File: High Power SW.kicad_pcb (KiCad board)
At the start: 2 copper layers, 48 x 48 mm, 19 parts

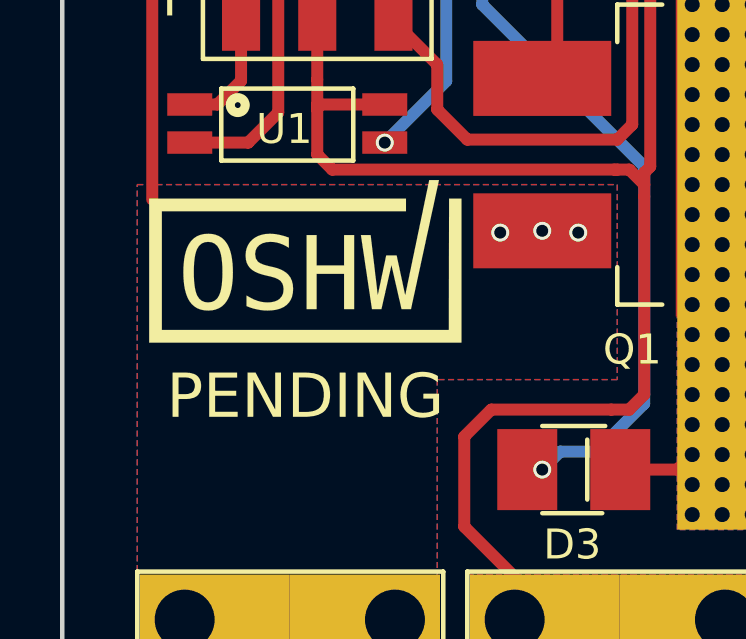
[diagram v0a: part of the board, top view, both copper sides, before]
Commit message: Maded Udates to silk
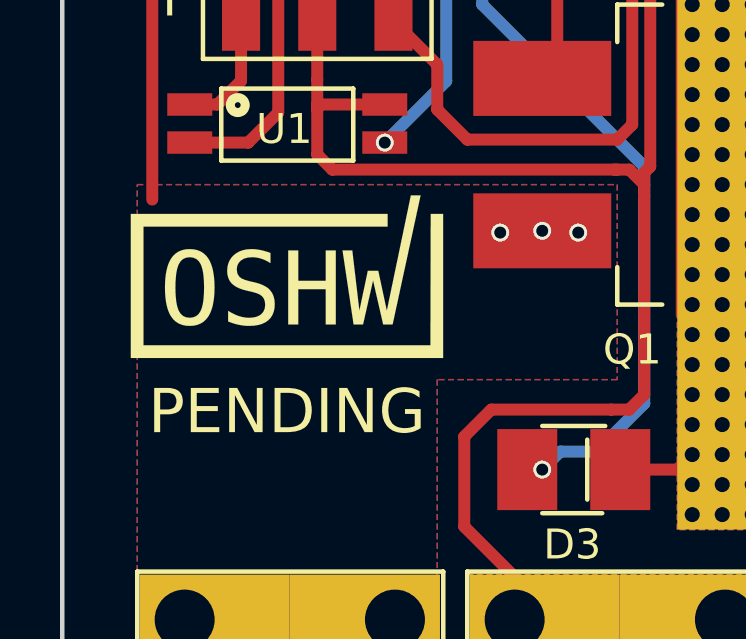
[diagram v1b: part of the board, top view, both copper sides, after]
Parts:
- added ?: , Symbols:OSHW-Logo2_14.6x12mm_SilkScreen, B.Cu at (79.9, 95.1)
- moved ? 1.85 mm to (79.9, 108.1)
- moved ? 0.80 mm to (74.6, 109.0)

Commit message: Updated Board
Changed connector type
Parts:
- removed the BED+ at (96.6, 125.4)
- removed the BED- at (107.6, 125.4)
- removed the POWER+ at (85.6, 125.4)
- removed the POWER- at (74.6, 125.4)
- added BED+: CONN_01X01, MyLib:Keystone_4966, F.Cu at (96.0, 126.0)
- added BED-: CONN_01X01, MyLib:Keystone_4966, F.Cu at (107.5, 126.0)
- added POWER+: CONN_01X01, MyLib:Keystone_4966, F.Cu at (86.0, 126.0)
- added POWER-: CONN_01X01, MyLib:Keystone_4966, F.Cu at (74.0, 126.0)
- CN1: value (none) -> Jumper_NC_Small
- D3: value (none) -> Led_Small
- Q1: value (none) -> IRFR7540TRPBF
- R1: value (none) -> 1.0K
- R2, R5: value (none) -> 1.8K
- R3: value (none) -> 300
- R4: value (none) -> 1.69K
- U1: value (none) -> PS2801C-1-A
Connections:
- CN1 pad 3: +BATT -> (no net)
- CN1 pad 4: GND -> (no net)
- CN1 pad 5: Net-(JP1-Pad1) -> (no net)
- CN1 pad 6: Net-(JP1-Pad2) -> (no net)

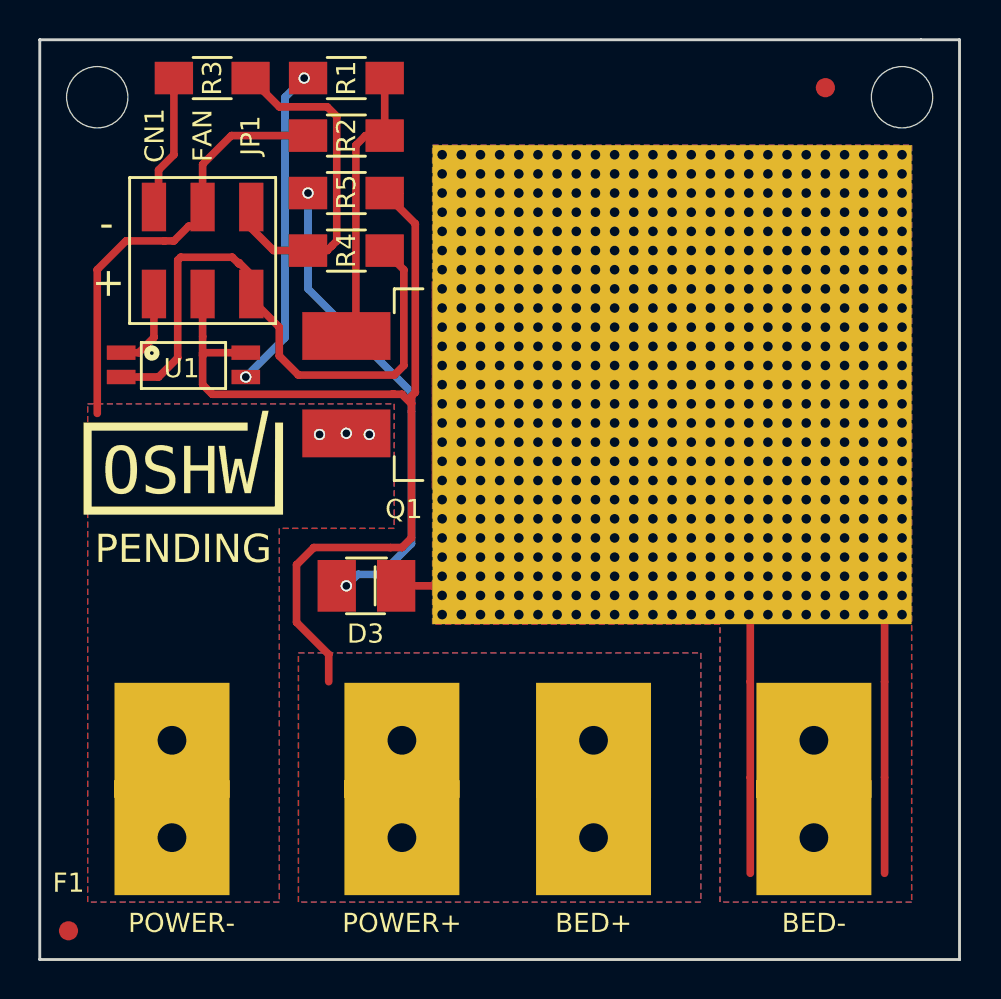
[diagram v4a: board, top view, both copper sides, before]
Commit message: Improved Board Size
Made the board smaller
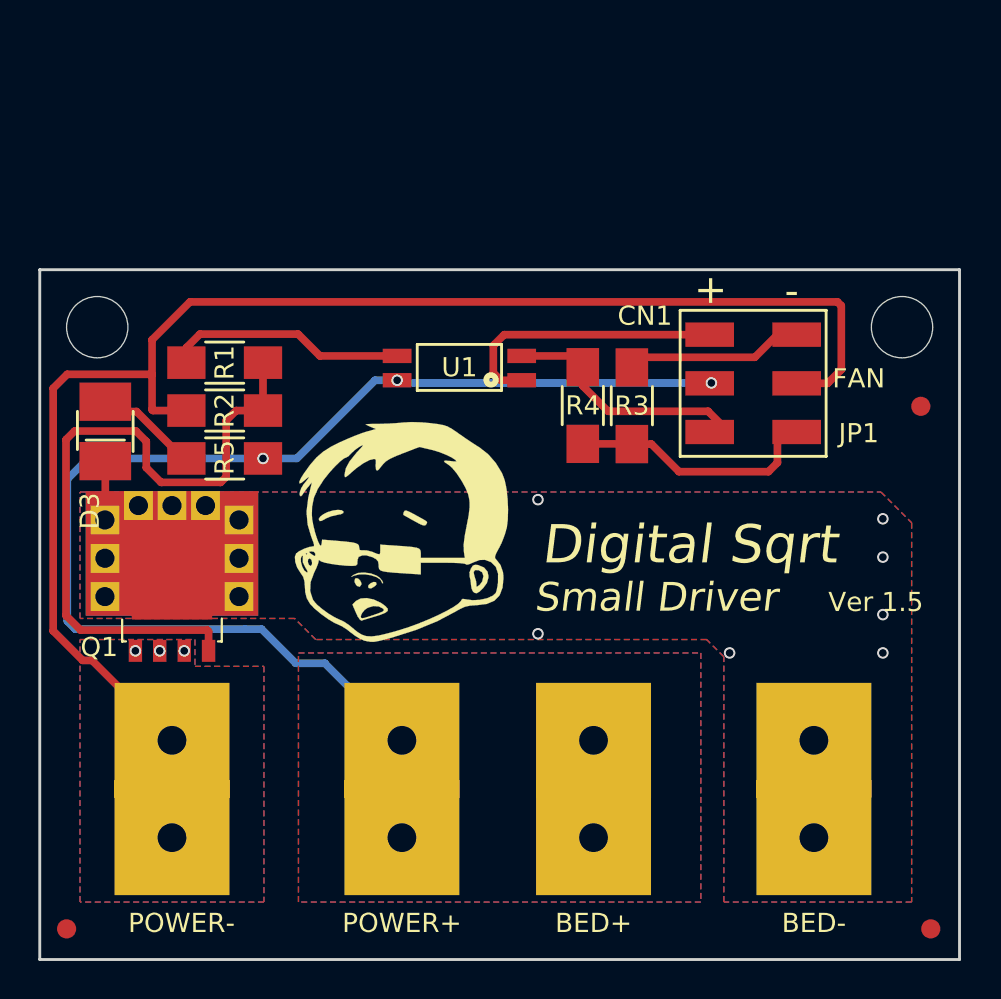
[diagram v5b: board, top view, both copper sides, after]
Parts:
- added F1 : , Fiducials:Fiducial_1mm_Dia_2.54mm_Outer_CopperTop, F.Cu at (113.6, 133.3)
- ?: moved to F.Cu
- ?: moved to B.Cu
- POWER-: footprint MyLib:Keystone_4966 -> Keystone_4966
- Q1: value IRFR7540TRPBF -> PSMN5R6-60YLX; footprint MyLib:TO-263-2Lead_(Larg_Heat_Sink) -> TO_SOT_Packages_SMD:SOT-669_LFPAK_ThermalVias-2
- R5: value 1.8K -> 3.6K
- moved CN1 29.6 mm to (104.3, 104.8), turned to 270 degrees
- moved ? 28.8 mm to (103.1, 112.9), turned to 180 degrees
- moved R3 27.8 mm to (98.0, 106.0), turned to 270 degrees
- moved ? 18.8 mm to (86.1, 112.9), turned to 180 degrees
- moved F2  17.4 mm to (113.1, 106.0)
- moved R1 16.2 mm to (76.8, 103.8)
- moved D3 15.8 mm to (70.5, 107.3), turned to 270 degrees
- moved R2 15.7 mm to (76.8, 106.2)
- moved R5 15.2 mm to (76.8, 108.8)
- moved R4 14.8 mm to (95.4, 106.0), turned to 90 degrees
- moved U1 14.4 mm to (89.0, 104.0), turned to 180 degrees
- moved Q1 13.6 mm to (74.0, 115.0), turned to 90 degrees
- moved ? 12.0 mm to (70.1, 101.9)
- moved ? 12.0 mm to (112.1, 101.9)
- moved ? 7.40 mm to (85.8, 112.5), turned to 0 degrees
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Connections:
- CN1 pad 3: (no net) -> +BATT
- CN1 pad 4: (no net) -> GND
- CN1 pad 5: (no net) -> Net-(JP1-Pad1)
- CN1 pad 6: (no net) -> Net-(JP1-Pad2)
- Q1 pad 1: Net-(Q1-Pad1) -> GND
- Q1 pad 4: Net-(BED-1-Pad1) -> Net-(Q1-Pad4)
- R1 pad 2: Net-(Q1-Pad1) -> Net-(Q1-Pad4)
- R2 pad 1: Net-(Q1-Pad1) -> Net-(Q1-Pad4)
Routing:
- net GND: track 28.0 -> 76.1 mm
- net Net-(Q1-Pad4): track 0.00 -> 36.1 mm
- net Net-(BED-1-Pad1): track 30.2 -> 3.61 mm, vias 0 -> 7
- net Net-(D3-Pad2): track 24.8 -> 6.02 mm, vias 2 -> 0
- net Net-(JP1-Pad1): track 31.5 -> 13.0 mm
- net Net-(Q1-Pad1): track 15.4 -> 0.00 mm
- net +BATT: track 52.4 -> 65.1 mm, vias 0 -> 3
- net Net-(CN1-Pad1): track 5.31 -> 15.6 mm
- net Net-(R1-Pad1): track 17.1 -> 12.5 mm, vias 2 -> 0
- net Net-(JP1-Pad2): track 17.4 -> 13.3 mm
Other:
- board size 48 x 48 mm -> 48 x 36 mm

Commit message: Reduced Board Size
Cleaned up the board and made it smaller
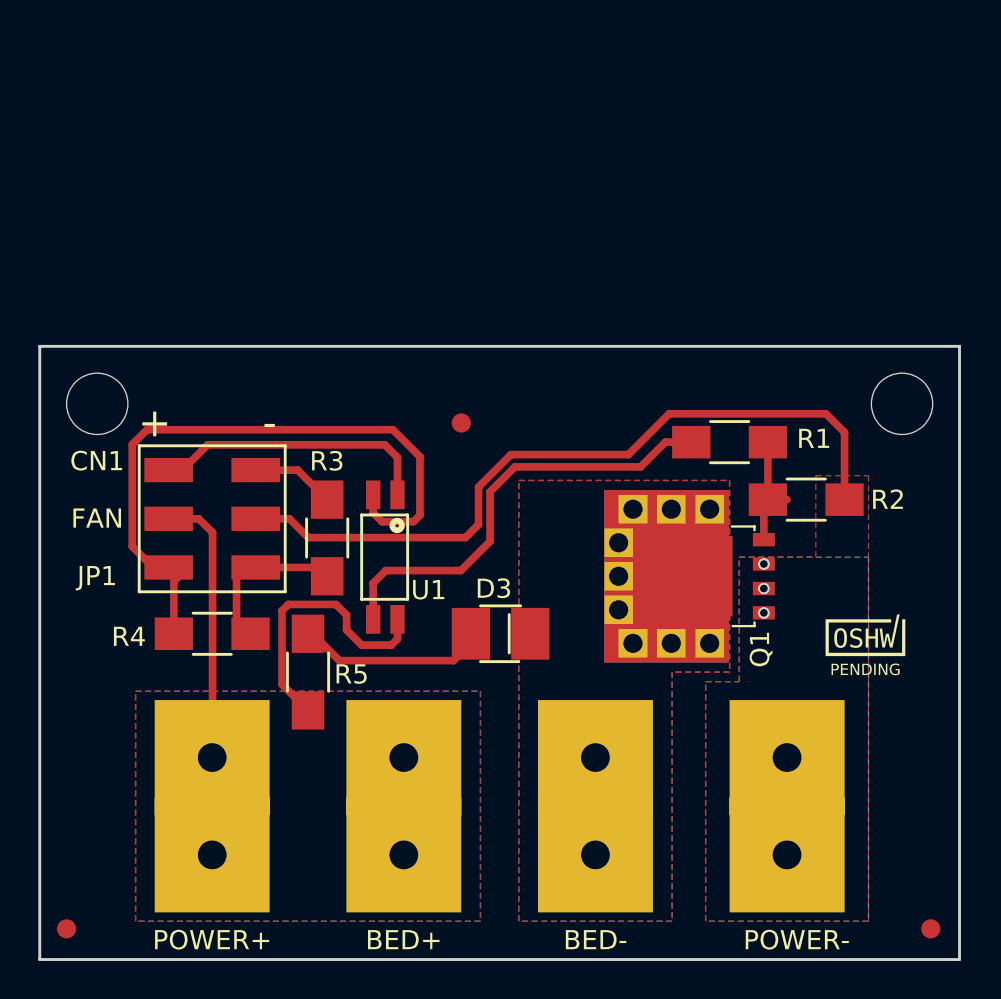
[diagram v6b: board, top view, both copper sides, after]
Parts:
- removed the ? at (103.1, 112.9)
- removed the ? at (86.1, 112.9)
- added OSHW_Mono_0.1_Scale: PENDING, kicad:OSHW_Mono_0.1_Scale, F.Cu at (110.2, 118.0)
- added REF***: OSHW-Logo2_9.8x8mm_SilkScreen, Symbols:OSHW-Logo2_9.8x8mm_SilkScreen, B.Cu at (77.6, 108.2)
- ?: moved to B.Cu
- F2: renamed from F1 
- F3: renamed from F2 
- moved POWER- 32.1 mm to (106.1, 126.9)
- moved R2 30.7 mm to (107.1, 110.9), turned to 0 degrees
- moved CN1 29.1 mm to (76.1, 111.9)
- moved Q1 27.1 mm to (101.1, 114.9), turned to 180 degrees
- moved R1 26.7 mm to (103.1, 107.9)
- moved F3 24.0 mm to (89.1, 106.9)
- moved D3 23.2 mm to (91.1, 117.9), turned to 0 degrees
- moved R4 22.7 mm to (76.1, 117.9), turned to 180 degrees
- moved R3 17.3 mm to (82.1, 112.9)
- moved R5 12.0 mm to (81.1, 119.9), turned to 90 degrees
- moved BED- 11.4 mm to (96.1, 126.9)
- moved U1 10.6 mm to (85.1, 113.9), turned to 270 degrees
- moved BED+ 9.94 mm to (86.1, 126.9)
- moved POWER+ 9.94 mm to (76.1, 126.9)
- moved ? 5.69 mm to (90.9, 115.1), turned to 180 degrees
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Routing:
- net +BATT: track 65.1 -> 27.8 mm, vias 3 -> 0
- net GND: track 76.1 -> 41.7 mm
- net Net-(Q1-Pad4): track 36.1 -> 6.18 mm
- net Net-(JP1-Pad1): track 13.0 -> 35.1 mm
- net Net-(R1-Pad1): track 12.5 -> 23.1 mm
- net Net-(JP1-Pad2): track 13.3 -> 8.68 mm
- net Net-(D3-Pad2): track 6.02 -> 10.2 mm
- net Net-(BED-1-Pad1): track 3.61 -> 0.00 mm, vias 7 -> 0
- net Net-(CN1-Pad2): track 8.31 -> 5.37 mm
- net Net-(CN1-Pad1): track 15.6 -> 13.9 mm
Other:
- board size 48 x 36 mm -> 48 x 32 mm
- board text added: "Ver 1.7"
- board text removed: "Ver 1.5"

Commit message: Changed back to orginal connectors
Changed back to orginal connectors.  They are more sturdy.
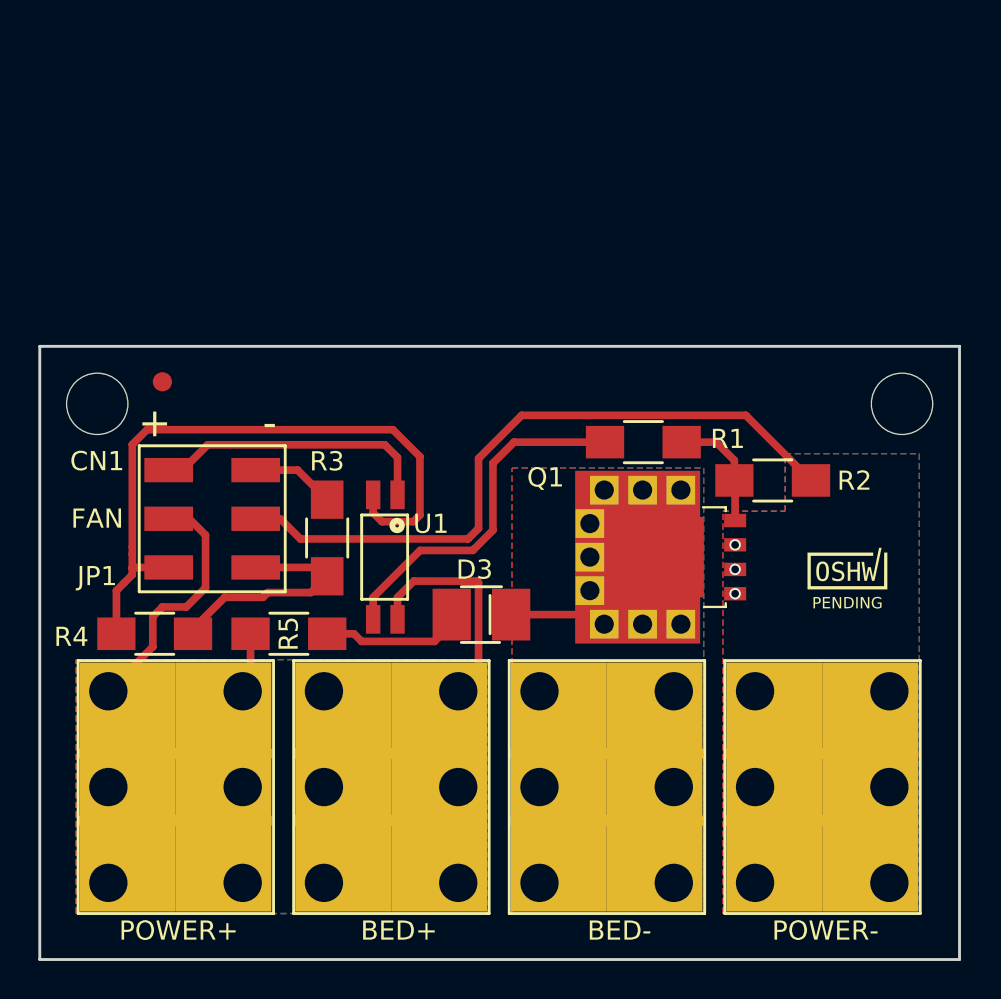
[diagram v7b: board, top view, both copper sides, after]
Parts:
- removed F2, F3: , Fiducials:Fiducial_1mm_Dia_2.54mm_Outer_CopperTop
- BED+, BED-, POWER+: footprint MyLib:Keystone_4966 -> MyLib:Keystone_terminal
- POWER-: footprint Keystone_4966 -> MyLib:Keystone_terminal
- moved REF*** 32.1 mm to (109.3, 112.9)
- moved F1  29.0 mm to (73.5, 104.8)
- moved ? 4.93 mm to (87.2, 111.8)
- moved R1 4.50 mm to (98.6, 107.9)
- moved OSHW_Mono_0.1_Scale 3.60 mm to (109.2, 114.5)
- moved R4 3.00 mm to (73.1, 117.9)
- moved POWER+ 2.24 mm to (74.1, 125.9)
- moved R5 2.24 mm to (80.1, 117.9), turned to 0 degrees
- moved POWER- 2.02 mm to (107.8, 125.9)
- moved R2 2.02 mm to (105.3, 109.9)
- moved Q1 1.80 mm to (99.6, 113.9)
- moved D3 1.41 mm to (90.1, 116.9)
- moved BED+ 1.25 mm to (85.3, 125.9)
- moved BED- 1.12 mm to (96.6, 125.9)
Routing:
- net Net-(BED-1-Pad1): track 0.00 -> 5.57 mm
- net Net-(JP1-Pad2): track 8.68 -> 13.3 mm
- net Net-(R1-Pad1): track 23.1 -> 18.7 mm
- net GND: track 41.7 -> 38.4 mm
- net Net-(JP1-Pad1): track 35.1 -> 37.8 mm
- net +BATT: track 27.8 -> 28.3 mm
- net Net-(D3-Pad2): track 10.2 -> 9.62 mm

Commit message: Fixed Silk
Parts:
- moved ? 2.20 mm to (89.3, 112.6)
- moved REF*** 1.91 mm to (108.5, 114.6)
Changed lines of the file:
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@@
   (page User 200 200)
   (layers
-    (0 F.Cu signal)
-    (31 B.Cu signal)
-    (35 F.Paste user)
+    (0 F.Cu signal hide)
+    (31 B.Cu signal hide)
+    (35 F.Paste user hide)
     (36 B.SilkS user)
-    (37 F.SilkS user)
+    (37 F.SilkS user hide)
     (38 B.Mask user)
-    (39 F.Mask user)
-    (40 Dwgs.User user)
+    (39 F.Mask user hide)
+    (40 Dwgs.User user hide)
     (44 Edge.Cuts user)
-    (45 Margin user)
+    (45 Margin user hide)
   )
   (setup
@@
   )
   (module MyLib:LOGO_POS (layer B.Cu)
-    (at 87.25 111.75 180)
+    (at 89.27 112.62 180)
     (attr smd)
     (fp_text reference "" (at 0.8 -7.4 180) (layer B.SilkS) hide
@@
   )
   (module Symbols:OSHW-Logo2_9.8x8mm_SilkScreen (layer B.Cu)
-    (at 109.35 112.9 180)
+    (at 108.47 114.6 180)
     (descr "Open Source Hardware Symbol")
     (tags "Logo Symbol OSHW")
@@
     (effects (font (size 2 2) (thickness 0.1)) (justify left))
   )
-  (gr_text "Small Driver" (at 81.5 116.75) (layer B.SilkS)
+  (gr_text "Small Driver" (at 83.02 116.47) (layer B.SilkS)
     (effects (font (size 1 1) (thickness 0.1) italic) (justify left mirror))
   )
-  (gr_text "Digital Sqrt" (at 81.5 114.5) (layer B.SilkS)
+  (gr_text "Digital Sqrt" (at 83.48 114.22) (layer B.SilkS)
     (effects (font (size 1.5 1.5) (thickness 0.2) italic) (justify left mirror))
   )
